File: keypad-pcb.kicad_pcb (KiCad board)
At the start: 2 copper layers, 72.4 x 83.1 mm, 32 parts, among them J1 AVR-ISP-6, K1 SW_Push, K2 SW_Push, K3 SW_Push, K4 SW_Push, K5 SW_Push, K6 SW_Push, SW0 RESET, U1 ATmega32U4-A, Y1 XTAL

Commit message: finish fills
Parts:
- moved C1 1.80 mm to (140.5, 108.2)
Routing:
- net +5V: track 152.8 -> 182.6 mm, vias 7 -> 8
- net GND: track 139.0 -> 164.8 mm, vias 3 -> 4
- net VCC: track 7.99 -> 18.8 mm, vias 0 -> 2
- net Net-(U1-UCAP): track 5.15 -> 6.98 mm
- net Net-(U1-~{HWB}/PE2): track 8.09 -> 8.62 mm

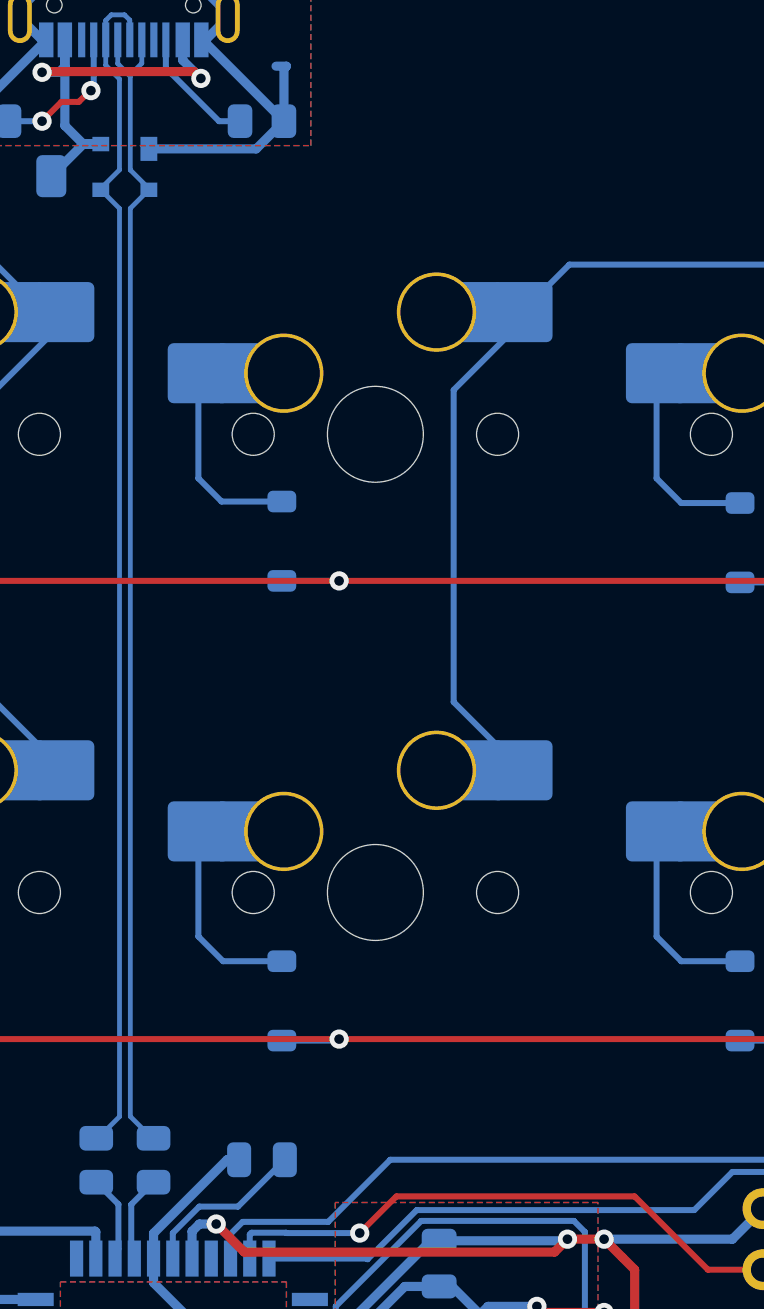
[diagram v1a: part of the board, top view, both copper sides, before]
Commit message: missing ground
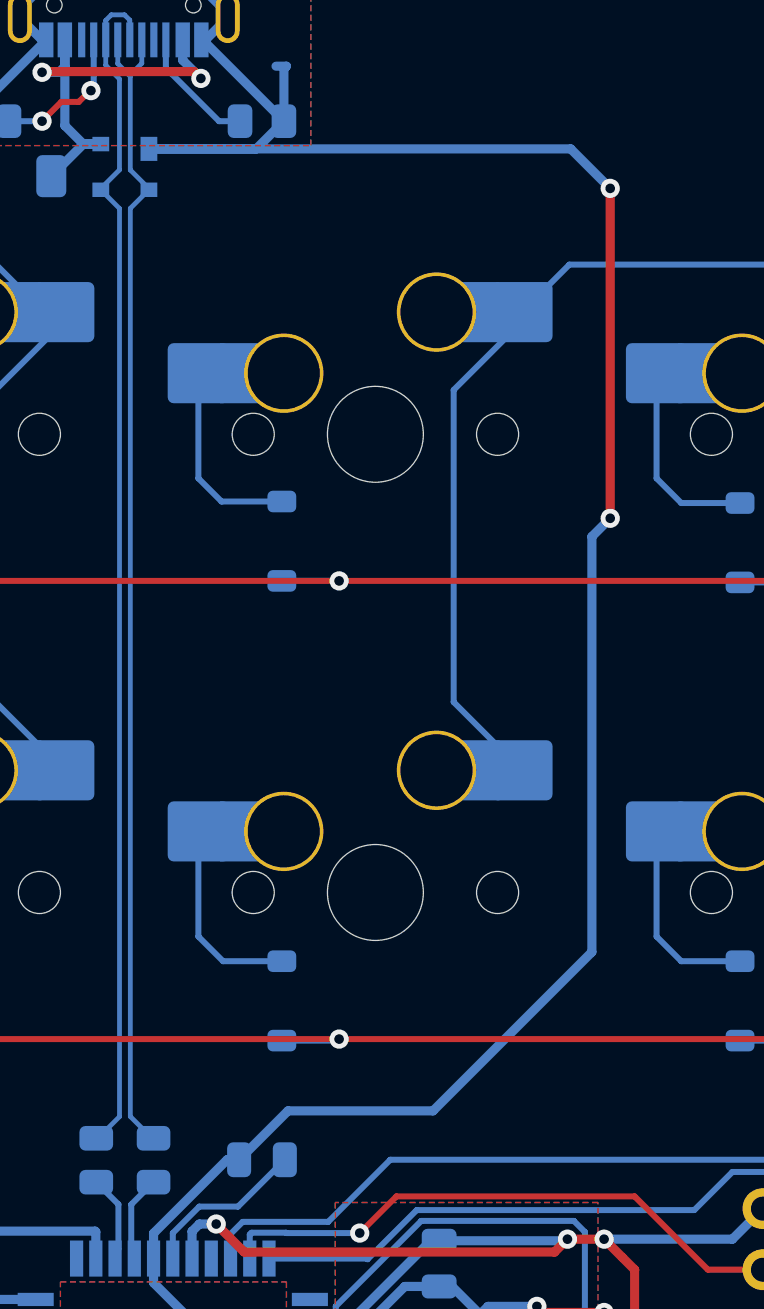
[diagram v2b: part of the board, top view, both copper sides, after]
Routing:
- net GND: track 164.8 -> 235.0 mm, vias 4 -> 6
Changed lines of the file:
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@@
   (segment (start 152.146 114.554) (end 151.892 114.3) (width 0.381) (layer "F.Cu") (net 1))
   (segment (start 154.686 114.554) (end 152.146 114.554) (width 0.381) (layer "F.Cu") (net 1))
+  (segment (start 154.94 67.818) (end 154.94 81.534) (width 0.381) (layer "F.Cu") (net 1))
   (segment (start 161.29 119.634) (end 161.29 115.316) (width 0.381) (layer "F.Cu") (net 1))
   (segment (start 156.464 124.46) (end 161.29 119.634) (width 0.381) (layer "F.Cu") (net 1))
@@
   (via (at 156.464 124.46) (size 0.8) (drill 0.4) (layers "F.Cu" "B.Cu") (net 1))
   (via (at 136.652 117.856) (size 0.8) (drill 0.4) (layers "F.Cu" "B.Cu") (free) (net 1))
+  (via (at 154.94 67.818) (size 0.8) (drill 0.4) (layers "F.Cu" "B.Cu") (net 1))
+  (via (at 154.94 81.534) (size 0.8) (drill 0.4) (layers "F.Cu" "B.Cu") (net 1))
   (via (at 154.686 114.554) (size 0.8) (drill 0.4) (layers "F.Cu" "B.Cu") (net 1))
   (segment (start 137.941 61.643) (end 137.9935 61.643) (width 0.381) (layer "B.Cu") (net 1))
   (segment (start 141.478 62.738) (end 141.3745 62.8415) (width 0.381) (layer "B.Cu") (net 1))
+  (segment (start 147.574 106.172) (end 141.544 106.172) (width 0.381) (layer "B.Cu") (net 1))
   (segment (start 145.962 117.006) (end 147.662 118.706) (width 0.381) (layer "B.Cu") (net 1))
   (segment (start 139.036 60.54542) (end 139.036 60.728) (width 0.381) (layer "B.Cu") (net 1))
+  (segment (start 154.178 82.296) (end 154.178 99.568) (width 0.381) (layer "B.Cu") (net 1))
   (segment (start 157.936 126.056) (end 156.655 126.056) (width 0.381) (layer "B.Cu") (net 1))
   (segment (start 139.036 60.728) (end 139.214 60.728) (width 0.381) (layer "B.Cu") (net 1))
   (segment (start 135.9536 113.318337) (end 135.9536 112.312337) (width 0.381) (layer "B.Cu") (net 1))
   (segment (start 139.012 108.204) (end 135.9536 111.2624) (width 0.381) (layer "B.Cu") (net 1))
+  (segment (start 153.298587 66.176587) (end 154.94 67.818) (width 0.381) (layer "B.Cu") (net 1))
   (segment (start 151.892 114.3) (end 149.86 114.3) (width 0.381) (layer "B.Cu") (net 1))
   (segment (start 141.3745 62.8415) (end 141.3745 65.024) (width 0.381) (layer "B.Cu") (net 1))
@@
   (segment (start 130.396 60.728) (end 130.396 60.358) (width 0.381) (layer "B.Cu") (net 1))
   (segment (start 141.666 124.624737) (end 140.7536 123.712337) (width 0.381) (layer "B.Cu") (net 1))
+  (segment (start 154.94 81.534) (end 154.178 82.296) (width 0.381) (layer "B.Cu") (net 1))
   (segment (start 147.828 113.472) (end 148.36275 113.472) (width 0.381) (layer "B.Cu") (net 1))
   (segment (start 140.7536 122.581337) (end 140.7536 123.712337) (width 0.381) (layer "B.Cu") (net 1))
   (segment (start 131.491 61.643) (end 131.491 61.6525) (width 0.381) (layer "B.Cu") (net 1))
   (segment (start 137.9935 61.643) (end 141.3745 65.024) (width 0.381) (layer "B.Cu") (net 1))
+  (segment (start 141.544 106.172) (end 139.512 108.204) (width 0.381) (layer "B.Cu") (net 1))
   (segment (start 142.4536 116.412337) (end 139.0476 116.412337) (width 0.381) (layer "B.Cu") (net 1))
   (segment (start 151.572 119.0625) (end 150.4565 117.947) (width 0.381) (layer "B.Cu") (net 1))
@@
   (segment (start 137.941 61.643) (end 138.121 61.643) (width 0.381) (layer "B.Cu") (net 1))
   (segment (start 130.396 56.548) (end 130.396 60.728) (width 0.381) (layer "B.Cu") (net 1))
+  (segment (start 135.76 66.176587) (end 153.298587 66.176587) (width 0.381) (layer "B.Cu") (net 1))
   (segment (start 148.36275 113.472) (end 149.525375 114.634625) (width 0.381) (layer "B.Cu") (net 1))
   (segment (start 147.828 113.472) (end 146.399937 113.472) (width 0.381) (layer "B.Cu") (net 1))
   (segment (start 151.572 116.68125) (end 150.30625 117.947) (width 0.381) (layer "B.Cu") (net 1))
+  (segment (start 154.178 99.568) (end 147.574 106.172) (width 0.381) (layer "B.Cu") (net 1))
   (segment (start 131.491 61.6525) (end 128.1195 65.024) (width 0.381) (layer "B.Cu") (net 1))
   (segment (start 128.016 63.5) (end 128.1195 63.6035) (width 0.381) (layer "B.Cu") (net 1))
